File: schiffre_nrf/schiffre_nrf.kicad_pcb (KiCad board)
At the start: 2 copper layers, 70 x 70 mm, 32 parts, among them J1 Conn_01x02, J2 Conn_01x04, J3 Conn_01x01_Pin, J4 Conn_01x04, J5 FH34SRJ-30S-0.5SH(50), P1 USB_C_Plug_USB2.0, Q1 AO3407, Q2 AO3407, U1 E73-2G4M08S1C, U2 XC6220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

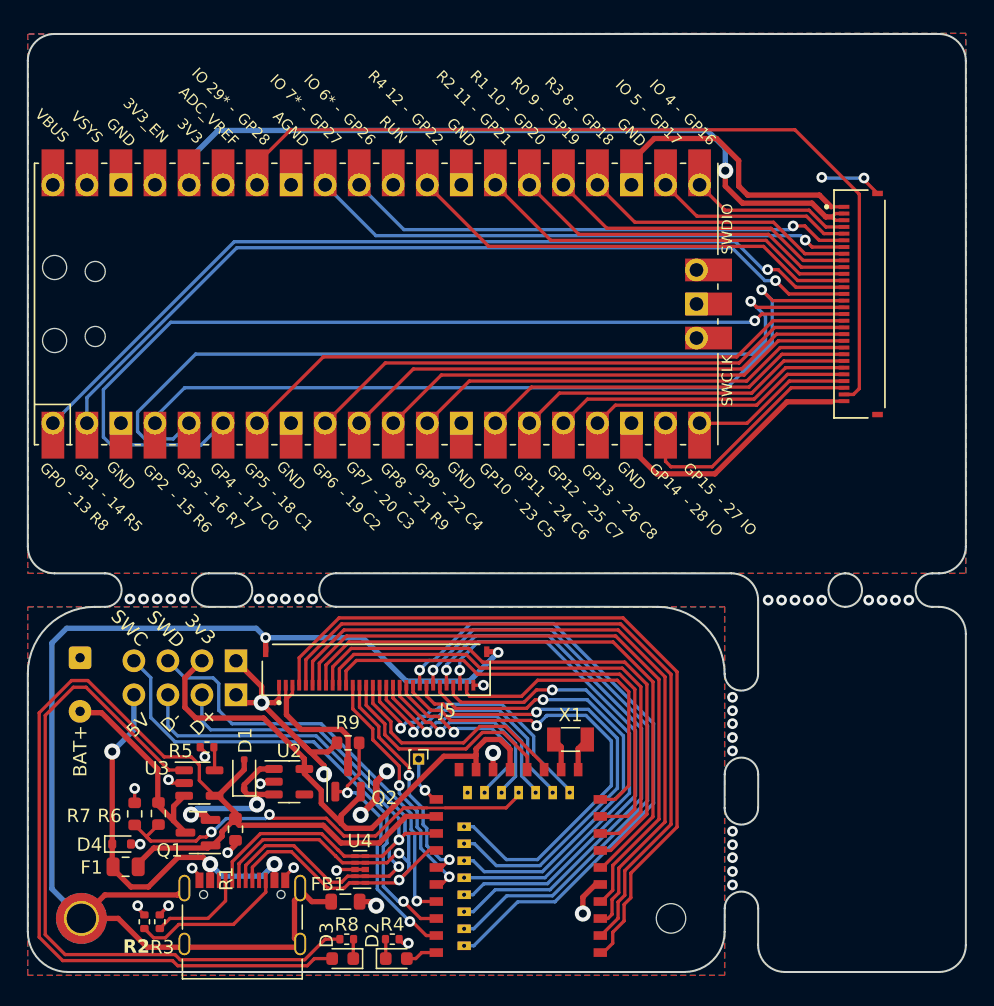
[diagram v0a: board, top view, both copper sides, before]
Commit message: factored out the pico breakout board
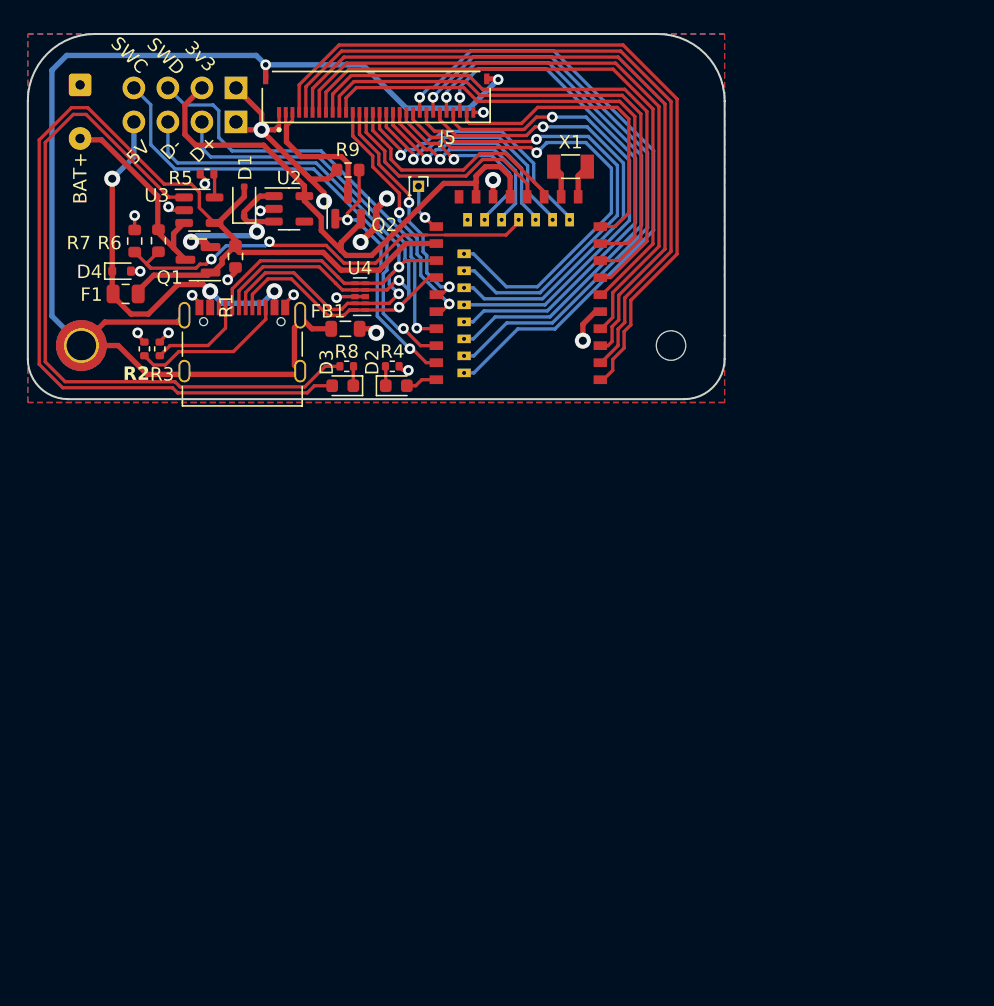
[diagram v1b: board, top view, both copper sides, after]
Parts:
- removed Jw1: FH34SRJ-30S-0.5SH(50), FH34SRJ-30S-05:HRS_FH34SRJ-30S-0.5SH(50)
- removed U5: Pico, RPi_Pico:RPi_Pico_SMD_TH
- moved F1 42.8 mm to (22.3, 34.1)
- moved P1 42.8 mm to (31.0, 37.7)
- moved R9 42.8 mm to (38.9, 24.9)
- moved U3 42.8 mm to (27.8, 27.9)
- moved X1 42.8 mm to (55.5, 24.6)
- moved D1 42.8 mm to (31.1, 27.2)
- moved D2 42.8 mm to (42.5, 41.0)
- moved D3 42.8 mm to (38.5, 41.0)
- moved D4 42.8 mm to (22.0, 32.5)
- moved FB1 42.8 mm to (38.7, 36.8)
- moved H1 42.8 mm to (19.0, 38.0)
- moved H2 42.8 mm to (63.0, 38.0)
- moved J1 42.8 mm to (18.9, 18.6)
- moved J2 42.8 mm to (30.5, 18.8)
- moved J3 42.8 mm to (44.2, 26.1)
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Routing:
- net /RPi Pico Breakout/GPIO4: track 71.0 -> 0.00 mm, vias 1 -> 0
- net /RPi Pico Breakout/GPIO0: track 66.1 -> 0.00 mm, vias 1 -> 0
- net /RPi Pico Breakout/GPIO3: track 65.6 -> 0.00 mm, vias 1 -> 0
- net /RPi Pico Breakout/GPIO28_ADC2: track 65.4 -> 0.00 mm
- net /RPi Pico Breakout/GPIO1: track 64.5 -> 0.00 mm, vias 1 -> 0
- net /RPi Pico Breakout/GPIO2: track 59.5 -> 0.00 mm, vias 1 -> 0
- net B_VEXT: track 57.1 -> 0.00 mm, vias 1 -> 0
- net B_GND: track 47.1 -> 0.00 mm, vias 2 -> 0
- net /RPi Pico Breakout/GPIO5: track 47.0 -> 0.00 mm
- net /RPi Pico Breakout/GPIO6: track 41.7 -> 0.00 mm
- net /RPi Pico Breakout/GPIO27_ADC1: track 40.6 -> 0.00 mm, vias 1 -> 0
- net /RPi Pico Breakout/GPIO7: track 38.9 -> 0.00 mm
- net /RPi Pico Breakout/GPIO26_ADC0: track 38.1 -> 0.00 mm, vias 1 -> 0
- net /RPi Pico Breakout/GPIO8: track 36.2 -> 0.00 mm
- net /RPi Pico Breakout/GPIO22: track 34.1 -> 0.00 mm
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- removed copper zone on B.Cu, net B_GND
- removed copper zone on F.Cu, net B_GND
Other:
- board size 70 x 70 mm -> 52 x 27.2 mm
- board text removed: "- 13 R8"
- board text removed: "- 14 R5"
- board text removed: "- 15 R6"
- board text removed: "- 16 R7"
- board text removed: "- 17 C0"
- board text removed: "- 18 C1"
- board text removed: "- 19 C2"
- board text removed: "- 20 C3"
- board text removed: "- 21 R9"
- board text removed: "- 22 C4"
- board text removed: "- 23 C5"
- board text removed: "- 24 C6"
- board text removed: "- 25 C7"
- board text removed: "- 26 C8"
- board text removed: "- 27 IO"
- board text removed: "- 28 IO"
- board text removed: "IO 29* -"
- board text removed: "IO 4 -"
- board text removed: "IO 5 -"
- board text removed: "IO 6* -"
- board text removed: "IO 7* -"
- board text removed: "R0 9 -"
- board text removed: "R1 10 -"
- board text removed: "R2 11 -"
- board text removed: "R3 8 -"
- board text removed: "R4 12 -"
